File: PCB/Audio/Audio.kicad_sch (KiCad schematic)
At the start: 46 parts, among them J1 Battery, J2 Reset, J3 TC2030-USB-NL-DS, J4 TF_PUSH, J5 USB-C-Socket-H, Q2 CJ2301, SW1 SW_Push, U1 R, U2 ESP32-S3-MINI-1, U2 L, U3 TP4054, U4 ME6211C33M5G-N

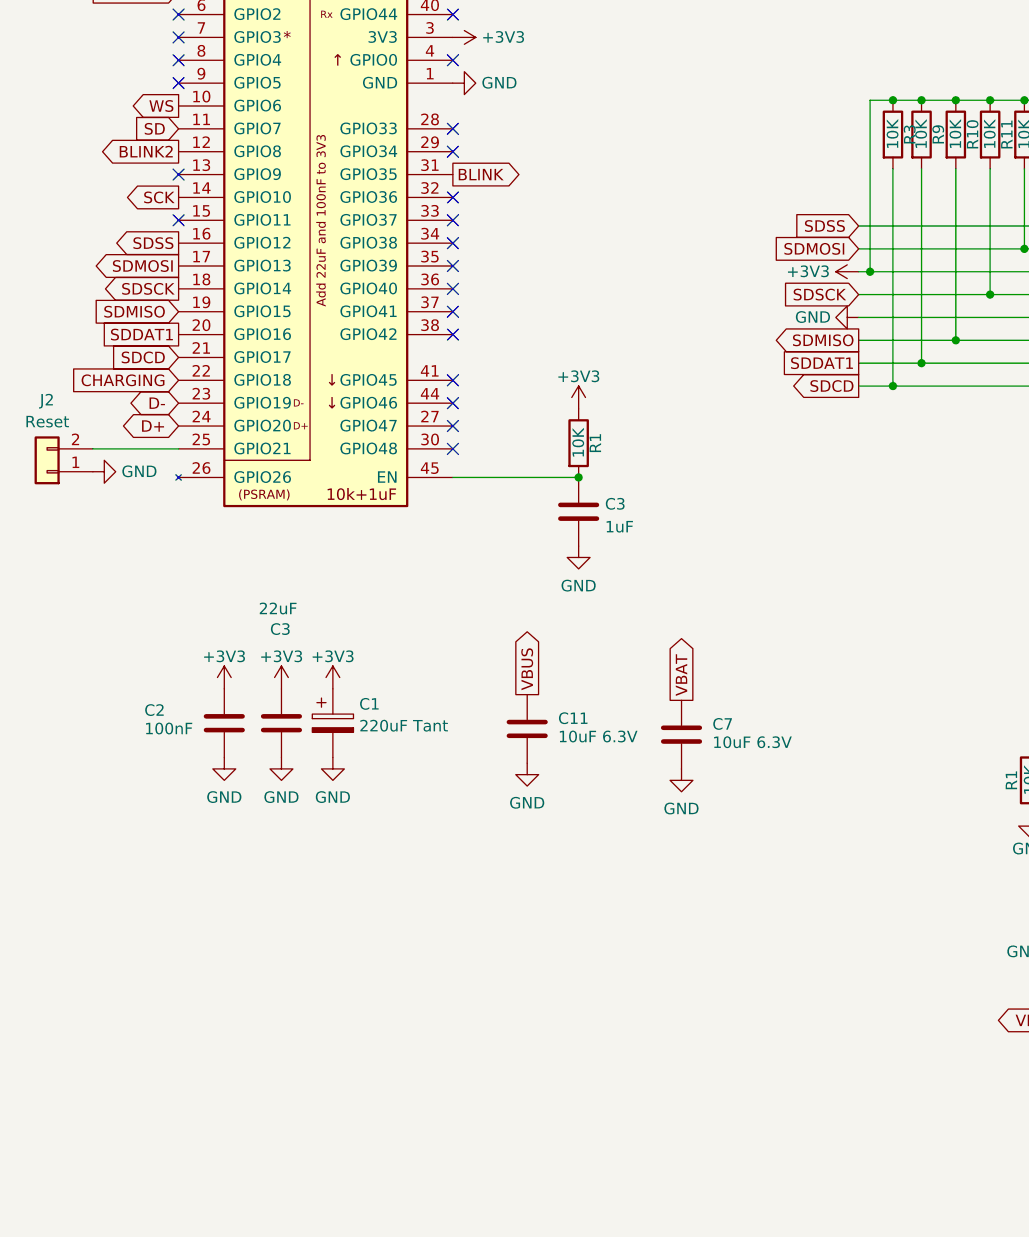
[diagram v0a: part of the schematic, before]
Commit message: Reworked to have speaker, and VBUS test.
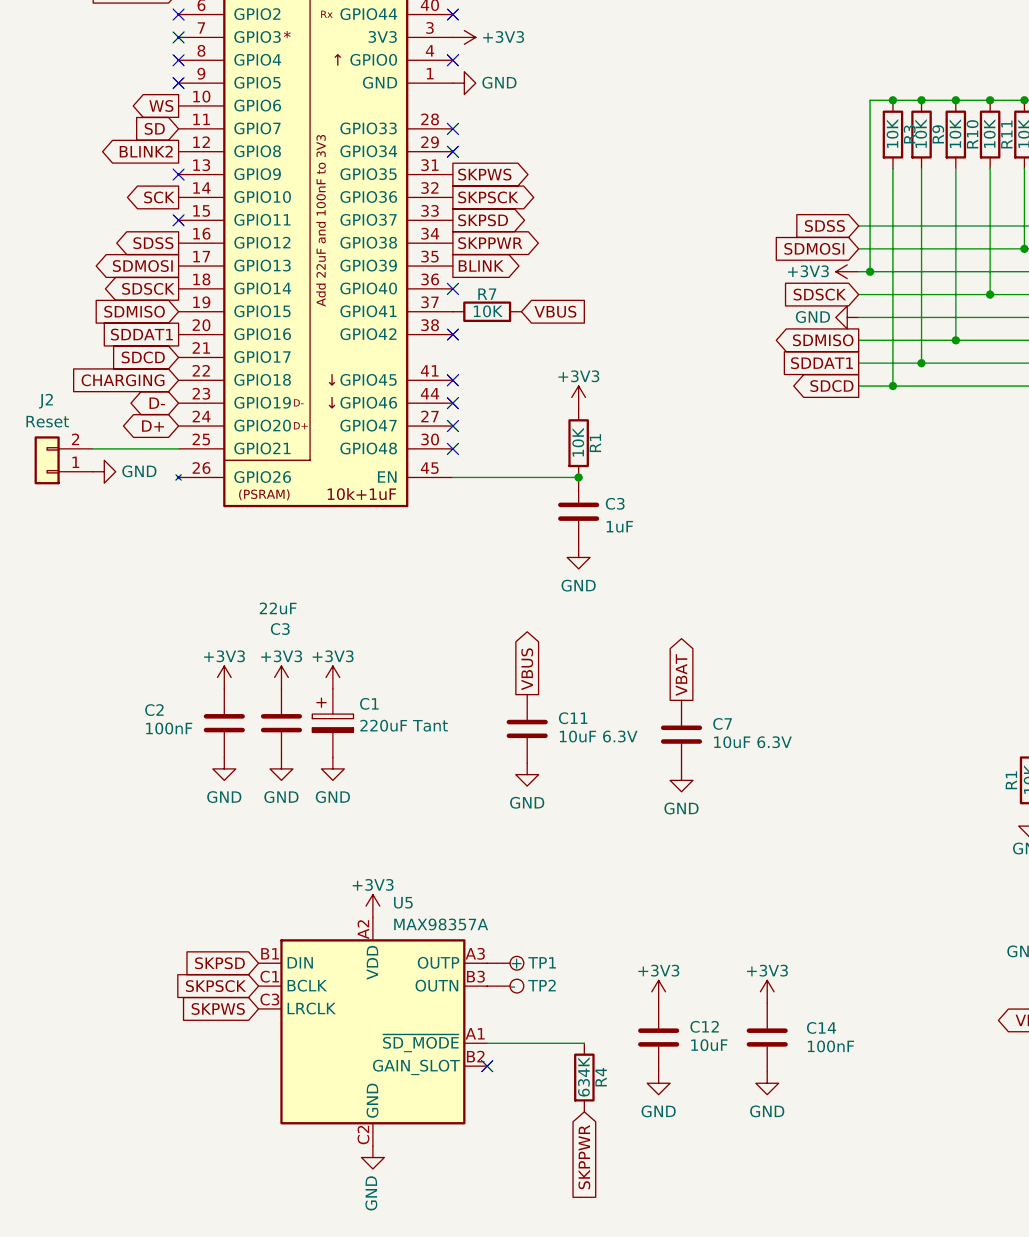
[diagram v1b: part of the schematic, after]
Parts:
- added C12: 10uF, RevK:C_0402, symbol Device:C
- added C14: 100nF, RevK:C_0402, symbol Device:C
- added R4: 634K, RevK:R_0402, symbol Device:R
- added R7: 10K, RevK:R_0402, symbol Device:R
- added TP1: +, RevK:SolderPadSmall, symbol Connector:TestPoint
- added TP2: -, RevK:SolderPadSmall, symbol Connector:TestPoint
- added U5: MAX98357A, RevK:WLP-1.437mmx1.347mm-0.21mm-ball, symbol RevK:MAX98357A
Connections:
- net +3V3: now also C12.1, C14.1, U5.A2 (VDD)
- net BLINK: now also U2.35 (GPIO39); no longer U2.31 (GPIO35)
- net GND: now also C12.2, C14.2, U5.C2 (GND)
- net VBUS: now also R7.2
- net SKPSCK: now reaches U2.32 (GPIO36)
- net SKPSCK: now also U5.C1 (BCLK)
- net SKPSD: now reaches U2.33 (GPIO37)
- net SKPSD: now also U5.B1 (DIN)
- net SKPPWR: now reaches U2.34 (GPIO38)
- net SKPPWR: now also R4.2
- net at U2.37 (GPIO41): now also R7.1
- new net: R4.1, U5.A1 (~{SD_MODE})
- new net: TP1.1, U5.A3 (OUTP)
- new net: TP2.1, U5.B3 (OUTN)
- new net SKPWS: U2.31 (GPIO35), U5.C3 (LRCLK)
- no-connect marks 24 -> 20

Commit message: Tidy
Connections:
- net GND: now also U5.B2 (GAIN_SLOT)
- no-connect marks 20 -> 19
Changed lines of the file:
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@@
 	)
 	(no_connect
-		(at 69.85 170.18)
-	)
-	(no_connect
 		(at 66.04 53.34)
 	)
@@
 					(unit 1)
 				)
+			)
+		)
+	)
+	(symbol
+		(lib_id "power:GND")
+		(at 69.85 170.18 90)
+		(mirror x)
+		(unit 1)
+		(exclude_from_sim no)
+		(in_bom yes)
+		(on_board yes)
+		(dnp no)
+		(property "Reference" "#PWR044"
+			(at 76.2 170.18 0)
+			(effects
+				(font
+					(size 1.27 1.27)
+				)
+				(hide yes)
+			)
+		)
+		(property "Value" "GND"
+			(at 73.1012 170.307 90)
+			(effects
+				(font
+					(size 1.27 1.27)
+				)
+				(justify right)
+			)
+		)
+		(property "Footprint" ""
+			(at 69.85 170.18 0)
+			(effects
+				(font
+					(size 1.27 1.27)
+				)
+				(hide yes)
+			)
+		)
+		(property "Datasheet" ""
+			(at 69.85 170.18 0)
+			(effects
+				(font
+					(size 1.27 1.27)
+				)
+				(hide yes)
+			)
+		)
+		(property "Description" ""
+			(at 69.85 170.18 0)
+			(effects
+				(font
+					(size 1.27 1.27)
+				)
+				(hide yes)
+			)
+		)
+		(pin "1"
+		)
+		(instances
+			(project "Audio"
+				(path "/46c350bb-7de4-4e81-aafd-4af55e37aab0"
+					(reference "#PWR044")
+					(unit 1)
+				)
